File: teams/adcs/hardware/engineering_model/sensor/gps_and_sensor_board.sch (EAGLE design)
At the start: 41 parts, among them U1 TPS732XX, U2 TPS732XX, U3 OEM719, U4 LTC3624

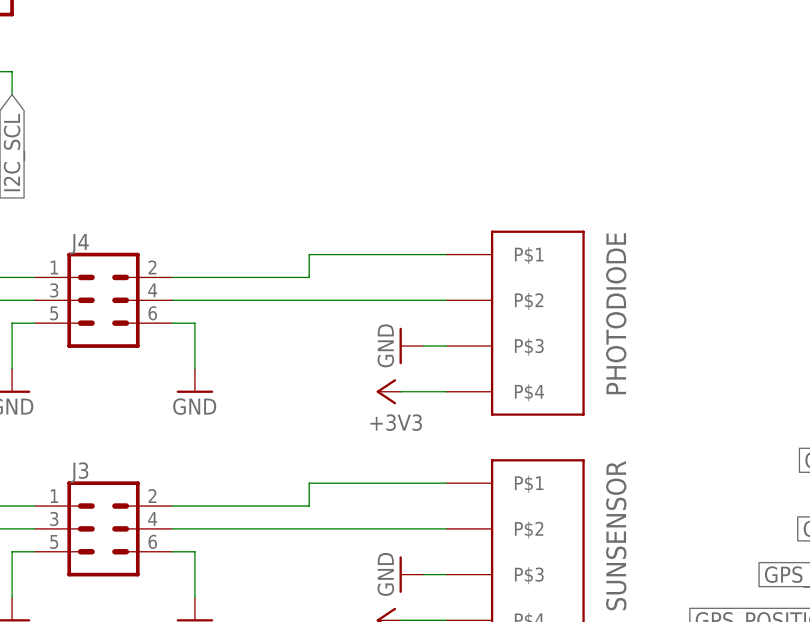
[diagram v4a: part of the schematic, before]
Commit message: ADCS/GPS: Add additional smoothing capacitor before sensors
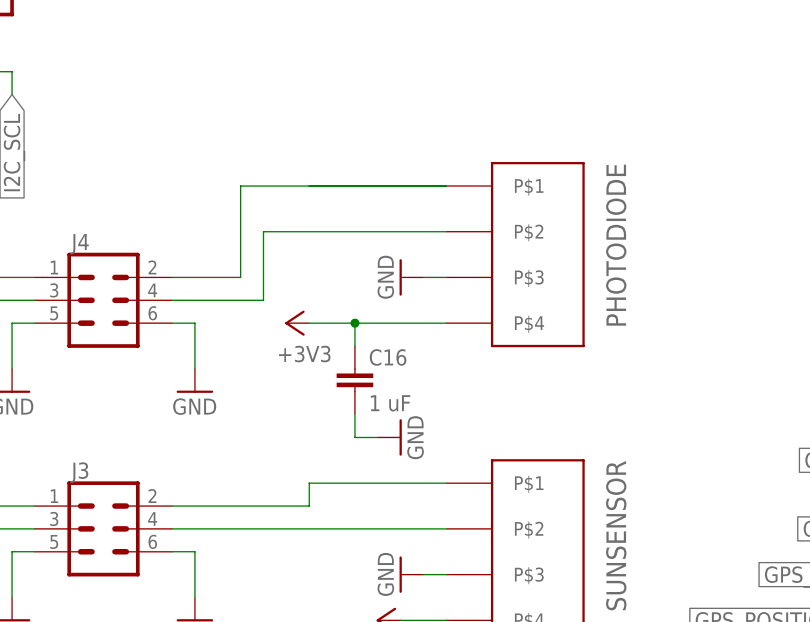
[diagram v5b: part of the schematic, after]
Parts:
- added C16: 1 uF, DubSat1 Components:CAPACITOR0805
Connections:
- net GND: now also C16.2
- net LDO_3V3: now also C16.1
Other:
- moved on the sheet: PHOTODIODE
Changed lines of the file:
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@@
 <part name="GND23" library="supply1" library_urn="urn:adsk.eagle:library:371" deviceset="GND" device=""/>
 <part name="GND24" library="supply1" library_urn="urn:adsk.eagle:library:371" deviceset="GND" device=""/>
+<part name="C16" library="DubSat1 Components" deviceset="CAPACITOR" device="0805" value="1 uF"/>
+<part name="GND25" library="supply1" library_urn="urn:adsk.eagle:library:371" deviceset="GND" device=""/>
 </parts>
 <sheets>
@@
 <instance part="C4" gate="G$1" x="180.34" y="15.24"/>
 <instance part="GND12" gate="1" x="180.34" y="22.86" rot="R180"/>
-<instance part="PHOTODIODE" gate="G$1" x="190.5" y="-55.88" rot="R270"/>
+<instance part="PHOTODIODE" gate="G$1" x="190.5" y="-48.26" rot="R270"/>
 <instance part="SUNSENSOR" gate="G$1" x="190.5" y="-81.28" rot="R270"/>
 <instance part="P+1" gate="1" x="-35.56" y="-40.64" rot="R90"/>
 <instance part="+3V31" gate="G$1" x="-35.56" y="-60.96" rot="R90"/>
 <instance part="GND1" gate="1" x="-22.86" y="-66.04" rot="R270"/>
-<instance part="GND4" gate="1" x="180.34" y="-53.34" rot="R270"/>
+<instance part="GND4" gate="1" x="180.34" y="-45.72" rot="R270"/>
 <instance part="GND5" gate="1" x="180.34" y="-78.74" rot="R270"/>
-<instance part="+3V34" gate="G$1" x="177.8" y="-58.42" rot="R90"/>
+<instance part="+3V34" gate="G$1" x="167.64" y="-50.8" rot="R90"/>
 <instance part="+3V35" gate="G$1" x="177.8" y="-83.82" rot="R90"/>
 <instance part="R1" gate="G$1" x="96.52" y="-38.1" rot="R270"/>
@@
 <instance part="GND23" gate="1" x="137.16" y="-58.42"/>
 <instance part="GND24" gate="1" x="157.48" y="-58.42"/>
+<instance part="C16" gate="G$1" x="175.26" y="-58.42"/>
+<instance part="GND25" gate="1" x="180.34" y="-63.5" rot="R90"/>
 </instances>
 <busses>
@@
 <pinref part="GND4" gate="1" pin="GND"/>
 <pinref part="PHOTODIODE" gate="G$1" pin="P$3"/>
-<wire x1="182.88" y1="-53.34" x2="185.42" y2="-53.34" width="0.1524" layer="91"/>
+<wire x1="182.88" y1="-45.72" x2="185.42" y2="-45.72" width="0.1524" layer="91"/>
 </segment>
 <segment>
@@
 <wire x1="157.48" y1="-76.2" x2="157.48" y2="-81.28" width="0.1524" layer="91"/>
 </segment>
+<segment>
+<pinref part="C16" gate="G$1" pin="2"/>
+<pinref part="GND25" gate="1" pin="GND"/>
+<wire x1="175.26" y1="-60.96" x2="175.26" y2="-63.5" width="0.1524" layer="91"/>
+<wire x1="175.26" y1="-63.5" x2="177.8" y2="-63.5" width="0.1524" layer="91"/>
+</segment>
 </net>
 <net name="VBAT" class="0">
@@
 <pinref part="PHOTODIODE" gate="G$1" pin="P$4"/>
 <pinref part="+3V34" gate="G$1" pin="+3V3"/>
-<wire x1="185.42" y1="-58.42" x2="180.34" y2="-58.42" width="0.1524" layer="91"/>
+<wire x1="185.42" y1="-50.8" x2="175.26" y2="-50.8" width="0.1524" layer="91"/>
+<pinref part="C16" gate="G$1" pin="1"/>
+<wire x1="175.26" y1="-50.8" x2="170.18" y2="-50.8" width="0.1524" layer="91"/>
+<wire x1="175.26" y1="-53.34" x2="175.26" y2="-50.8" width="0.1524" layer="91"/>
+<junction x="175.26" y="-50.8"/>
 </segment>
 <segment>
@@
 <pinref part="J4" gate="G$1" pin="4"/>
 <pinref part="PHOTODIODE" gate="G$1" pin="P$2"/>
-<wire x1="154.94" y1="-48.26" x2="185.42" y2="-48.26" width="0.1524" layer="91"/>
+<wire x1="154.94" y1="-48.26" x2="165.1" y2="-48.26" width="0.1524" layer="91"/>
+<wire x1="165.1" y1="-48.26" x2="165.1" y2="-40.64" width="0.1524" layer="91"/>
+<wire x1="165.1" y1="-40.64" x2="185.42" y2="-40.64" width="0.1524" layer="91"/>
 </segment>
 </net>
@@
 <segment>
 <pinref part="J4" gate="G$1" pin="2"/>
-<wire x1="154.94" y1="-45.72" x2="170.18" y2="-45.72" width="0.1524" layer="91"/>
-<wire x1="170.18" y1="-45.72" x2="170.18" y2="-43.18" width="0.1524" layer="91"/>
 <pinref part="PHOTODIODE" gate="G$1" pin="P$1"/>
-<wire x1="170.18" y1="-43.18" x2="185.42" y2="-43.18" width="0.1524" layer="91"/>
-</segment>
-</net>
+<wire x1="170.18" y1="-35.56" x2="185.42" y2="-35.56" width="0.1524" layer="91"/>
+<wire x1="154.94" y1="-45.72" x2="162.56" y2="-45.72" width="0.1524" layer="91"/>
+<wire x1="162.56" y1="-45.72" x2="162.56" y2="-35.56" width="0.1524" layer="91"/>
+<wire x1="162.56" y1="-35.56" x2="185.42" y2="-35.56" width="0.1524" layer="91"/>
+</segment>
+</net>

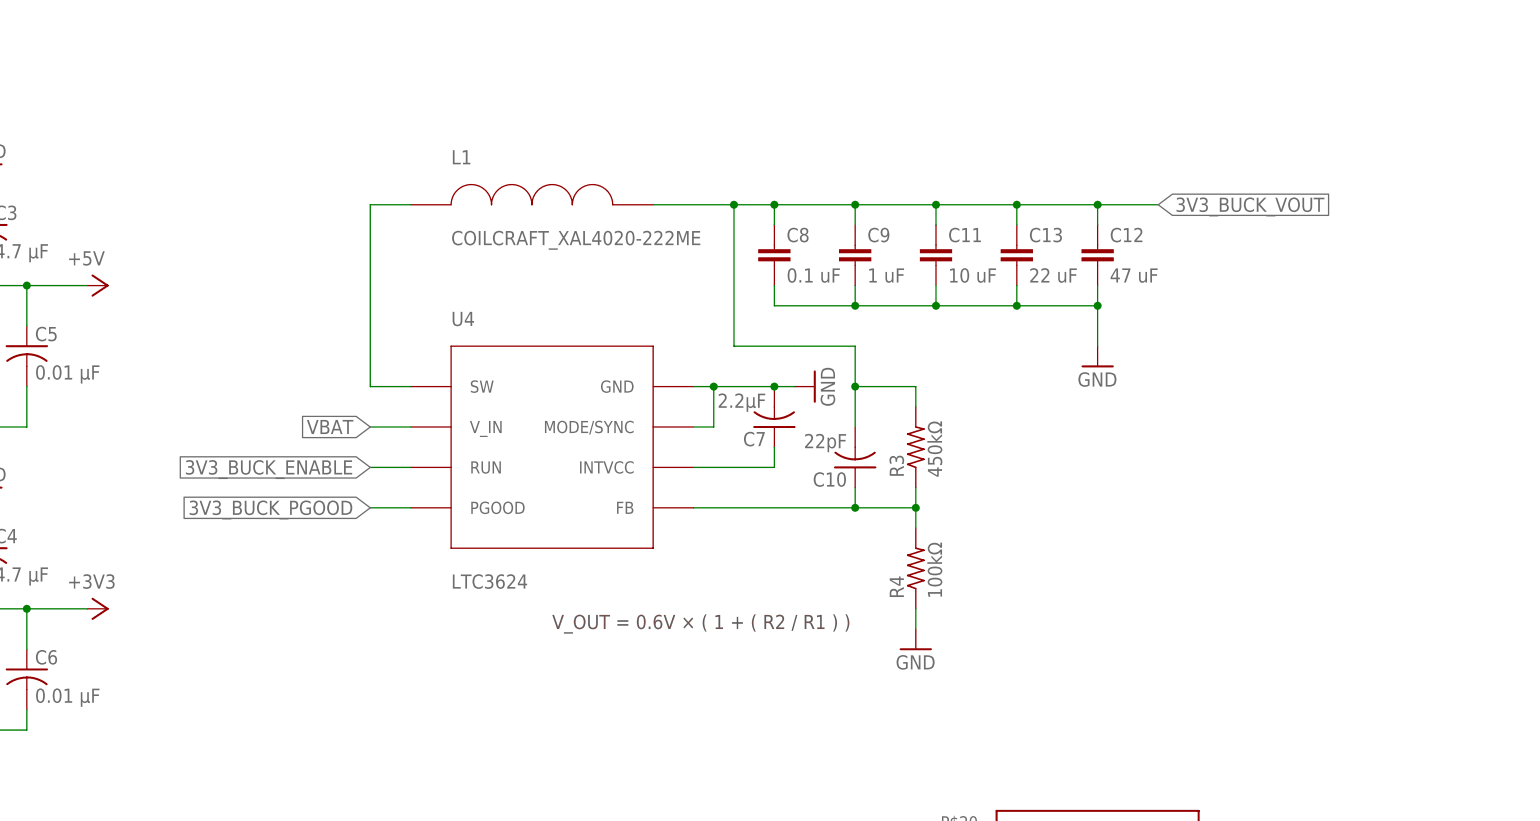
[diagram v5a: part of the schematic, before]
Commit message: ADCS/GPS: Update GPS footprint and begin rerouting
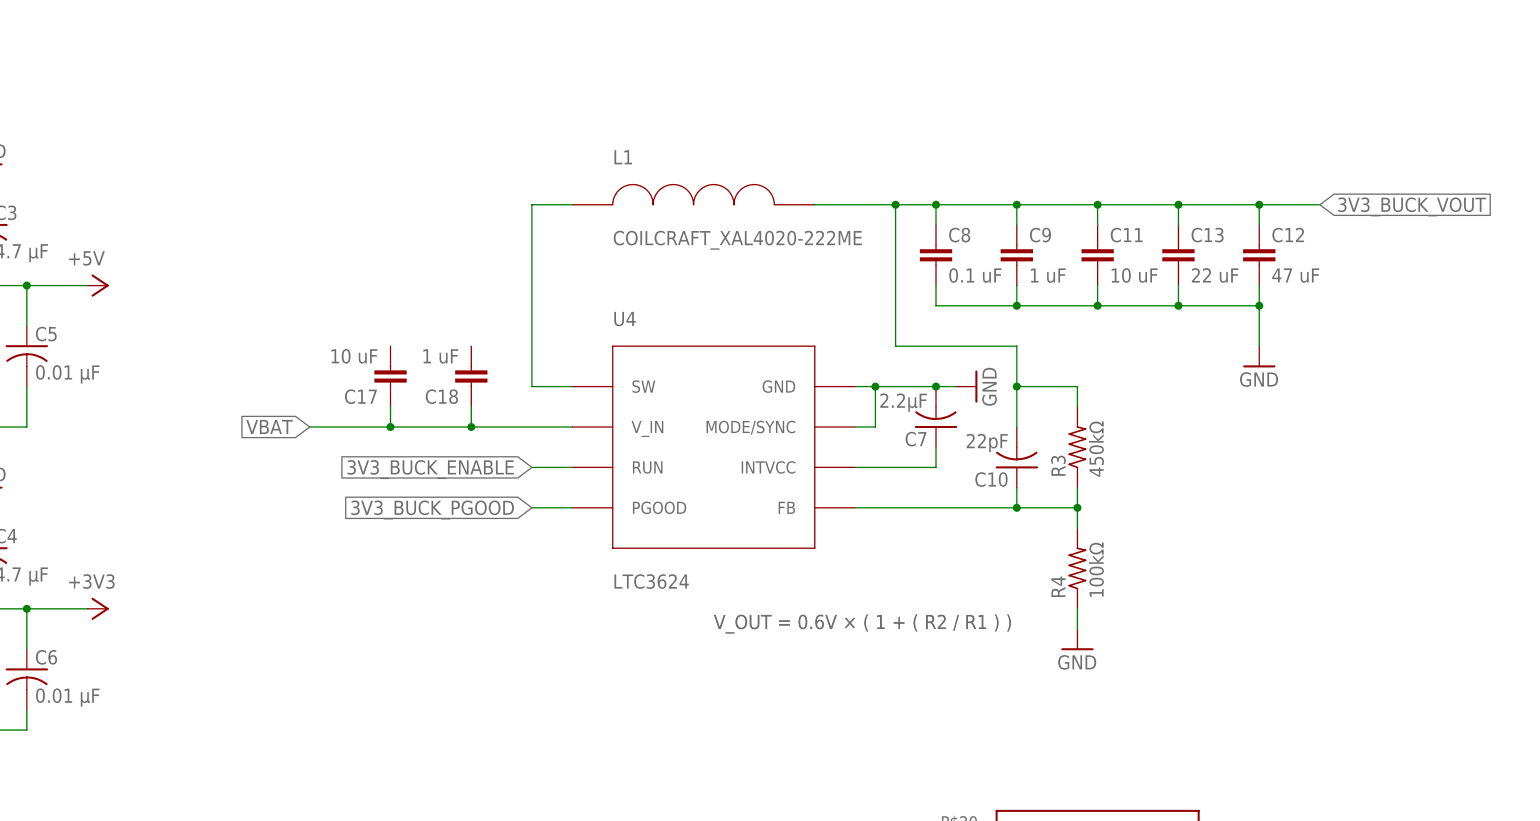
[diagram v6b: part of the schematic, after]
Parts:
- added C17: 10 uF, DubSat1 Components:CAPACITOR0805
- added C18: 1 uF, DubSat1 Components:CAPACITOR0805
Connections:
- net VBAT: now also C17.1, C18.1
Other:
- moved on the sheet: C10, C11, C12, C13, C7, C8, C9, L1, R3, R4, U4

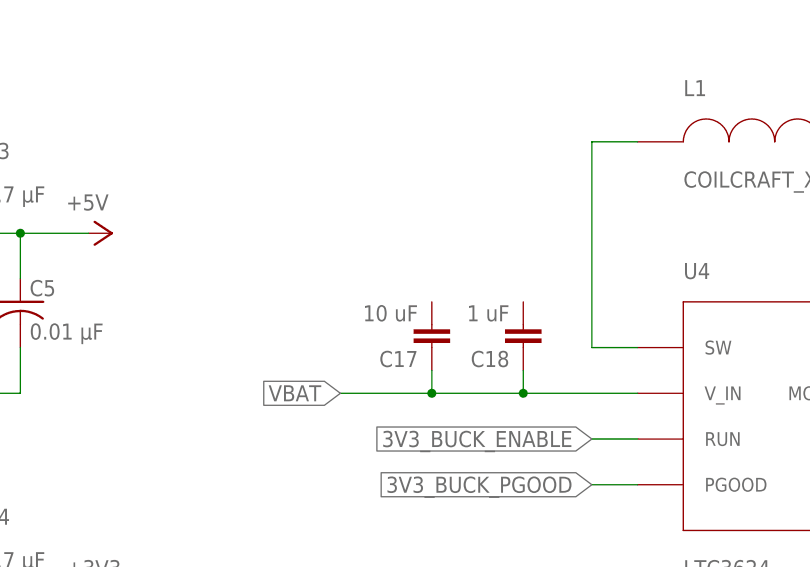
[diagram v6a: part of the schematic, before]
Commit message: ADCS/GPS: Add input capacitance to 3v3 buck
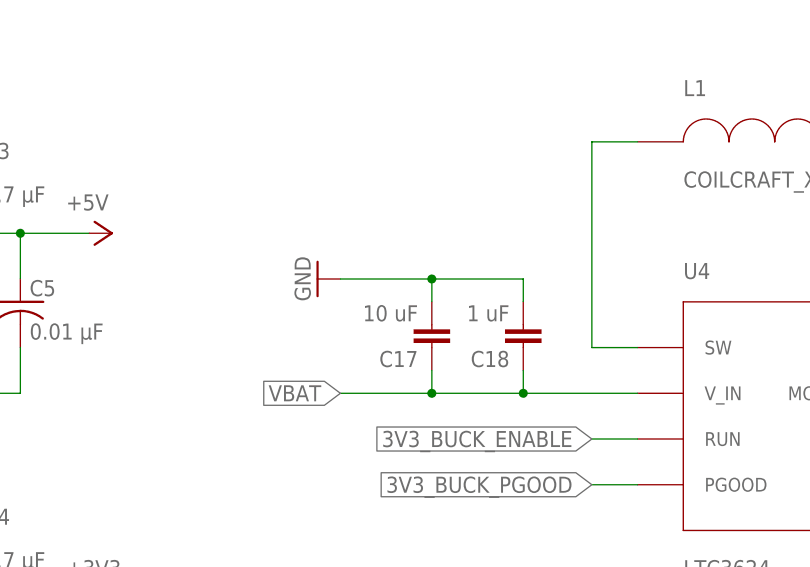
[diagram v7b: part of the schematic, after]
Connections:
- net GND: now also C17.2, C18.2
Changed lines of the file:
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@@
 <?xml version="1.0" encoding="utf-8"?>
 <!DOCTYPE eagle SYSTEM "eagle.dtd">
-<eagle version="8.5.2">
+<eagle version="8.5.0">
 <drawing>
 <settings>
@@
 <part name="C17" library="DubSat1 Components" deviceset="CAPACITOR" device="0805" value="10 uF"/>
 <part name="C18" library="DubSat1 Components" deviceset="CAPACITOR" device="0805" value="1 uF"/>
+<part name="GND26" library="supply1" library_urn="urn:adsk.eagle:library:371" deviceset="GND" device=""/>
 </parts>
 <sheets>
@@
 <instance part="C17" gate="G$1" x="231.14" y="38.1" rot="R180"/>
 <instance part="C18" gate="G$1" x="241.3" y="38.1" rot="R180"/>
+<instance part="GND26" gate="1" x="218.44" y="43.18" rot="R270"/>
 </instances>
 <busses>
@@
 <wire x1="175.26" y1="-63.5" x2="177.8" y2="-63.5" width="0.1524" layer="91"/>
 </segment>
+<segment>
+<pinref part="GND26" gate="1" pin="GND"/>
+<pinref part="C17" gate="G$1" pin="2"/>
+<wire x1="220.98" y1="43.18" x2="231.14" y2="43.18" width="0.1524" layer="91"/>
+<wire x1="231.14" y1="43.18" x2="231.14" y2="40.64" width="0.1524" layer="91"/>
+<pinref part="C18" gate="G$1" pin="2"/>
+<wire x1="231.14" y1="43.18" x2="241.3" y2="43.18" width="0.1524" layer="91"/>
+<wire x1="241.3" y1="43.18" x2="241.3" y2="40.64" width="0.1524" layer="91"/>
+<junction x="231.14" y="43.18"/>
+</segment>
 </net>
